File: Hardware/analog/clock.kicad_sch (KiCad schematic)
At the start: 4 parts, among them Y701 25MHz

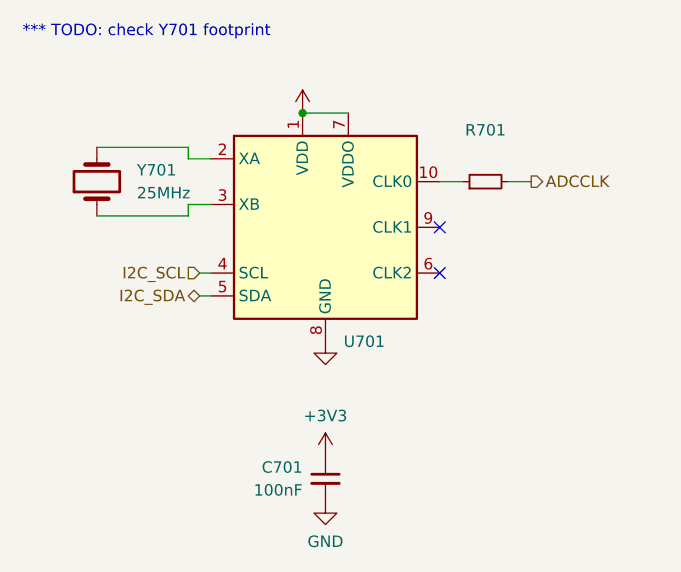
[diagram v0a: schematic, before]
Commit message: Add ADC aliasing filters
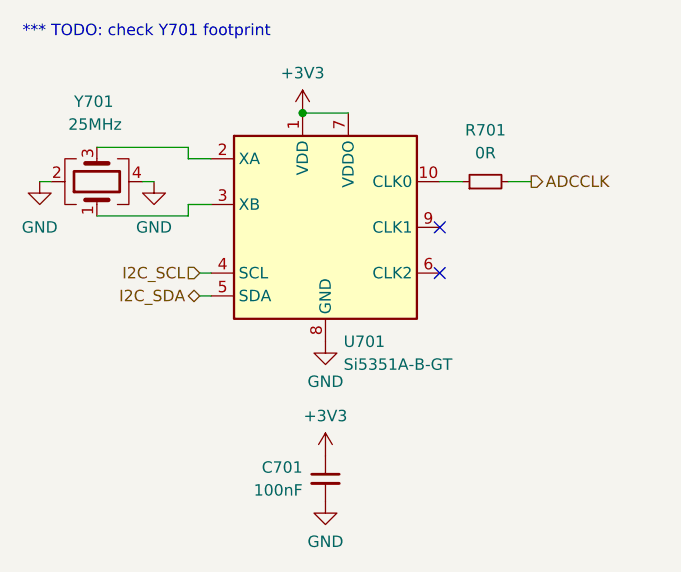
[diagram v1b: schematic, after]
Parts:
- R701: value (none) -> 0R; footprint (none) -> Resistor_SMD:R_0805_2012Metric_Pad1.20x1.40mm_HandSolder
- U701: value (none) -> Si5351A-B-GT; footprint (none) -> Package_SO:MSOP-10_3x3mm_P0.5mm
- Y701: symbol Device:Crystal -> Device:Crystal_GND24
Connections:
- net GND: now also Y701.2, Y701.4
- net at U701.2 (XA): now also Y701.3; no longer Y701.2
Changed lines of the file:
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@@
+    (stroke (width 0) (type default) (color 0 0 0 0))
+  )
+  (wire (pts (xy 29.21 36.83) (xy 30.48 36.83))
     (stroke (width 0) (type default) (color 0 0 0 0))
   )
@@
   )
   (wire (pts (xy 81.28 36.83) (xy 83.82 36.83))
+    (stroke (width 0) (type default) (color 0 0 0 0))
+  )
+  (wire (pts (xy 41.91 36.83) (xy 40.64 36.83))
     (stroke (width 0) (type default) (color 0 0 0 0))
   )
@@
       (effects (font (size 1.27 1.27)) hide)
     )
-    (property "Value" "" (id 1) (at 58.42 24.765 0))
+    (property "Value" "+3V3" (id 1) (at 58.42 24.765 0))
     (property "Footprint" "" (id 2) (at 58.42 29.21 0)
       (effects (font (size 1.27 1.27)) hide)
@@
     (in_bom yes) (on_board yes) (fields_autoplaced)
     (property "Reference" "R701" (id 0) (at 78.74 31.115 90))
-    (property "Value" "" (id 1) (at 78.74 33.655 90))
-    (property "Footprint" "" (id 2) (at 78.74 36.83 0)
+    (property "Value" "0R" (id 1) (at 78.74 33.655 90))
+    (property "Footprint" "Resistor_SMD:R_0805_2012Metric_Pad1.20x1.40mm_HandSolder" (id 2) (at 78.74 36.83 0)
       (effects (font (size 1.27 1.27)) hide)
     )
@@
     (pin "2")
   )
-  (symbol (lib_id "Device:Crystal") (at 35.56 36.83 90) (unit 1)
+  (symbol (lib_id "power:GND") (at 41.91 36.83 0) (mirror y) (unit 1)
     (in_bom yes) (on_board yes) (fields_autoplaced)
-    (property "Reference" "Y701" (id 0) (at 40.005 35.5599 90)
+    (property "Reference" "#PWR0117" (id 0) (at 41.91 43.18 0)
+      (effects (font (size 1.27 1.27)) hide)
+    )
+    (property "Value" "GND" (id 1) (at 41.91 41.91 0))
+    (property "Footprint" "" (id 2) (at 41.91 36.83 0)
+      (effects (font (size 1.27 1.27)) hide)
+    )
+    (property "Datasheet" "" (id 3) (at 41.91 36.83 0)
+      (effects (font (size 1.27 1.27)) hide)
+    )
+    (pin "1")
+  )
+  (symbol (lib_id "Device:Crystal_GND24") (at 35.56 36.83 90) (unit 1)
+    (in_bom yes) (on_board yes)
+    (property "Reference" "Y701" (id 0) (at 33.02 27.94 90)
       (effects (font (size 1.27 1.27)) (justify right))
     )
-    (property "Value" "25MHz" (id 1) (at 40.005 38.0999 90)
+    (property "Value" "25MHz" (id 1) (at 32.385 30.48 90)
       (effects (font (size 1.27 1.27)) (justify right))
     )
@@
     (pin "1")
     (pin "2")
+    (pin "3")
+    (pin "4")
+  )
+  (symbol (lib_id "power:GND") (at 29.21 36.83 0) (unit 1)
+    (in_bom yes) (on_board yes) (fields_autoplaced)
+    (property "Reference" "#PWR0112" (id 0) (at 29.21 43.18 0)
+      (effects (font (size 1.27 1.27)) hide)
+    )
+    (property "Value" "GND" (id 1) (at 29.21 41.91 0))
+    (property "Footprint" "" (id 2) (at 29.21 36.83 0)
+      (effects (font (size 1.27 1.27)) hide)
+    )
+    (property "Datasheet" "" (id 3) (at 29.21 36.83 0)
+      (effects (font (size 1.27 1.27)) hide)
+    )
+    (pin "1")
   )
   (symbol (lib_id "power:GND") (at 60.96 54.61 0) (unit 1)
@@
       (effects (font (size 1.27 1.27)) hide)
     )
-    (property "Value" "" (id 1) (at 60.96 59.055 0))
+    (property "Value" "GND" (id 1) (at 60.96 59.055 0))
     (property "Footprint" "" (id 2) (at 60.96 54.61 0)
       (effects (font (size 1.27 1.27)) hide)
@@
       (effects (font (size 1.27 1.27)) (justify left))
     )
-    (property "Value" "" (id 1) (at 62.9794 57.15 0)
+    (property "Value" "Si5351A-B-GT" (id 1) (at 62.9794 57.15 0)
       (effects (font (size 1.27 1.27)) (justify left))
     )
-    (property "Footprint" "" (id 2) (at 60.96 62.23 0)
+    (property "Footprint" "Package_SO:MSOP-10_3x3mm_P0.5mm" (id 2) (at 60.96 62.23 0)
       (effects (font (size 1.27 1.27)) hide)
     )

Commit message: Initial pass at analog board
- Everything currently in the schematic is routed, and stuff is
  reasonably sanely laid out

- Some compromises: namely, the zero offset doesn't use the DAC
  reference for its positive, but generates a separate 2.5V via the
  shunt diodes; this is then shared between both op-amps. That avoids
  the DAC/ADC reference getting noisified

  Also, we don't have an ADC for measuring the temperature sensors yet,
  and in fact, those aren't routed out (or existent really) yet either

- TODO: add test points for drive voltages and current sense voltages
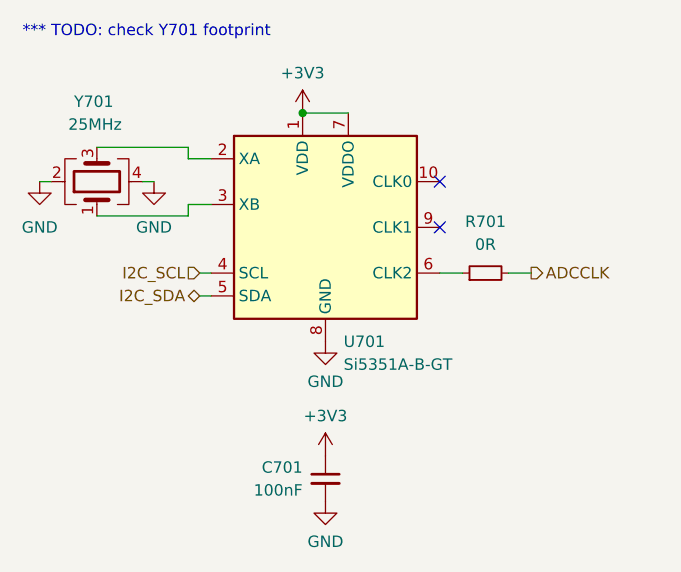
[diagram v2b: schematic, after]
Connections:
- net at R701.1: now also U701.6 (CLK2); no longer U701.10 (CLK0)
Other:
- title: (none) -> 300W Analog Load Board
- moved on the sheet: R701
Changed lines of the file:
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@@
 (kicad_sch (version 20211123) (generator eeschema)
   (paper "A4")
+  (title_block
+    (title "300W Analog Load Board")
+    (rev "1")
+  )
   (junction (at 58.42 29.21) (diameter 0) (color 0 0 0 0)
   )
-  (no_connect (at 73.66 46.99))
   (no_connect (at 73.66 41.91))
+  (no_connect (at 73.66 36.83))
   (wire (pts (xy 45.72 39.37) (xy 48.26 39.37))
     (stroke (width 0) (type default) (color 0 0 0 0))
@@
     (stroke (width 0) (type default) (color 0 0 0 0))
   )
-  (wire (pts (xy 81.28 36.83) (xy 83.82 36.83))
+  (wire (pts (xy 81.28 46.99) (xy 83.82 46.99))
     (stroke (width 0) (type default) (color 0 0 0 0))
   )
   (wire (pts (xy 41.91 36.83) (xy 40.64 36.83))
-    (stroke (width 0) (type default) (color 0 0 0 0))
-  )
-  (wire (pts (xy 73.66 36.83) (xy 76.2 36.83))
     (stroke (width 0) (type default) (color 0 0 0 0))
   )
@@
   )
   (wire (pts (xy 58.42 29.21) (xy 63.5 29.21))
+    (stroke (width 0) (type default) (color 0 0 0 0))
+  )
+  (wire (pts (xy 73.66 46.99) (xy 76.2 46.99))
     (stroke (width 0) (type default) (color 0 0 0 0))
   )
@@
     (effects (font (size 1.27 1.27)) (justify right))
   )
-  (hierarchical_label "ADCCLK" (shape output) (at 83.82 36.83 0)
+  (hierarchical_label "ADCCLK" (shape output) (at 83.82 46.99 0)
     (effects (font (size 1.27 1.27)) (justify left))
   )
@@
     (pin "2")
   )
-  (symbol (lib_id "Device:R_Small") (at 78.74 36.83 90) (unit 1)
+  (symbol (lib_id "Device:R_Small") (at 78.74 46.99 90) (unit 1)
     (in_bom yes) (on_board yes) (fields_autoplaced)
-    (property "Reference" "R701" (id 0) (at 78.74 31.115 90))
-    (property "Value" "0R" (id 1) (at 78.74 33.655 90))
-    (property "Footprint" "Resistor_SMD:R_0805_2012Metric_Pad1.20x1.40mm_HandSolder" (id 2) (at 78.74 36.83 0)
+    (property "Reference" "R701" (id 0) (at 78.74 41.275 90))
+    (property "Value" "0R" (id 1) (at 78.74 43.815 90))
+    (property "Footprint" "Resistor_SMD:R_0805_2012Metric_Pad1.20x1.40mm_HandSolder" (id 2) (at 78.74 46.99 0)
       (effects (font (size 1.27 1.27)) hide)
     )
-    (property "Datasheet" "~" (id 3) (at 78.74 36.83 0)
+    (property "Datasheet" "~" (id 3) (at 78.74 46.99 0)
       (effects (font (size 1.27 1.27)) hide)
     )

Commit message: Added more decoupling for reference
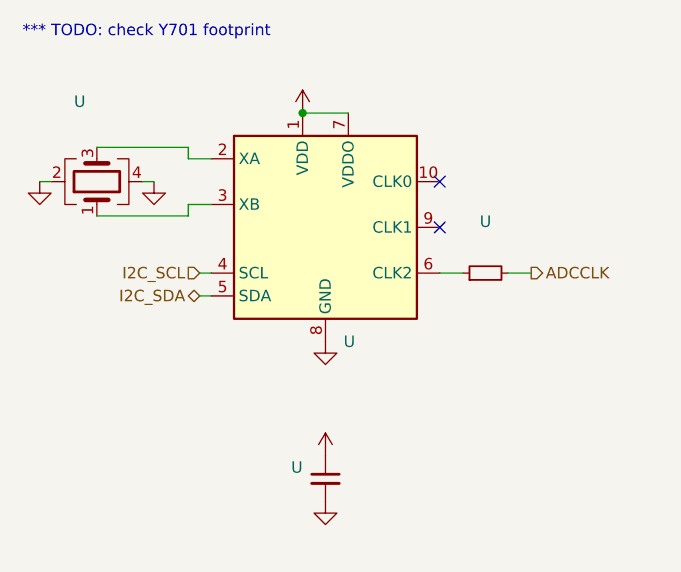
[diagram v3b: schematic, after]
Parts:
- U: renamed from C701; value 100nF -> (none); footprint Capacitor_SMD:C_0805_2012Metric_Pad1.18x1.45mm_HandSolder -> (none)
- U: renamed from R701; value 0R -> (none); footprint Resistor_SMD:R_0805_2012Metric_Pad1.20x1.40mm_HandSolder -> (none)
- U: renamed from Y701; value 25MHz -> (none); footprint Crystal:Crystal_SMD_SeikoEpson_TSX3225-4Pin_3.2x2.5mm_HandSoldering -> (none)
- U: renamed from U701; value Si5351A-B-GT -> (none); footprint Package_SO:MSOP-10_3x3mm_P0.5mm -> (none)

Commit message: Analog board layout
- Started work on adding the voltage sense circuitry, including the
  selector relay, IO expander to drive the relay, and the second ADC to
  convert the voltage values

- Changed the layout of analog board to better take advantage of
  available space

- Minor changes to front panel layout for aesthetics
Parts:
- added U: (no value), symbol Device:R_Small
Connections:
- net at U.9 (CLK1): now also U.1
- net ADCCLK renamed ADCCLK_{0}
- new net ADCCLK_{1}: U.2
- no-connect marks 2 -> 1
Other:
- moved on the sheet: U
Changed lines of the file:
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@@
   (junction (at 58.42 29.21) (diameter 0) (color 0 0 0 0)
   )
-  (no_connect (at 73.66 41.91))
   (no_connect (at 73.66 36.83))
   (wire (pts (xy 45.72 39.37) (xy 48.26 39.37))
+    (stroke (width 0) (type default))
+  )
+  (wire (pts (xy 73.66 46.99) (xy 74.93 46.99))
     (stroke (width 0) (type default))
   )
@@
     (stroke (width 0) (type default))
   )
-  (wire (pts (xy 81.28 46.99) (xy 83.82 46.99))
+  (wire (pts (xy 81.28 49.53) (xy 83.82 49.53))
     (stroke (width 0) (type default))
   )
@@
     (stroke (width 0) (type default))
   )
+  (wire (pts (xy 74.93 46.99) (xy 74.93 49.53))
+    (stroke (width 0) (type default))
+  )
   (wire (pts (xy 46.99 49.53) (xy 48.26 49.53))
+    (stroke (width 0) (type default))
+  )
+  (wire (pts (xy 74.93 49.53) (xy 76.2 49.53))
     (stroke (width 0) (type default))
   )
@@
     (stroke (width 0) (type default))
   )
-  (wire (pts (xy 73.66 46.99) (xy 76.2 46.99))
+  (wire (pts (xy 81.28 41.91) (xy 83.82 41.91))
     (stroke (width 0) (type default))
   )
   (wire (pts (xy 45.72 40.64) (xy 45.72 39.37))
+    (stroke (width 0) (type default))
+  )
+  (wire (pts (xy 73.66 41.91) (xy 76.2 41.91))
     (stroke (width 0) (type default))
   )
@@
     (effects (font (size 1.27 1.27)) (justify left bottom))
   )
+  (hierarchical_label "ADCCLK_{1}" (shape output) (at 83.82 41.91 0) (fields_autoplaced)
+    (effects (font (size 1.27 1.27)) (justify left))
+  )
   (hierarchical_label "I2C_SDA" (shape bidirectional) (at 46.99 49.53 180) (fields_autoplaced)
     (effects (font (size 1.27 1.27)) (justify right))
@@
     (effects (font (size 1.27 1.27)) (justify right))
   )
-  (hierarchical_label "ADCCLK" (shape output) (at 83.82 46.99 0) (fields_autoplaced)
+  (hierarchical_label "ADCCLK_{0}" (shape output) (at 83.82 49.53 0) (fields_autoplaced)
     (effects (font (size 1.27 1.27)) (justify left))
   )
@@
     (pin "2")
   )
-  (symbol (lib_id "Device:R_Small") (at 78.74 46.99 90) (unit 1)
-    (in_bom yes) (on_board yes) (fields_autoplaced)
+  (symbol (lib_id "Device:R_Small") (at 78.74 41.91 90) (unit 1)
+    (in_bom yes) (on_board yes)
     (default_instance (reference "U") (unit 1) (value "") (footprint ""))
-    (property "Reference" "U" (id 0) (at 78.74 41.275 90)
+    (property "Reference" "U" (id 0) (at 78.74 37.465 90)
       (effects (font (size 1.27 1.27)))
     )
-    (property "Value" "" (id 1) (at 78.74 43.815 90)
+    (property "Value" "" (id 1) (at 78.74 40.005 90)
       (effects (font (size 1.27 1.27)))
     )
-    (property "Footprint" "" (id 2) (at 78.74 46.99 0)
+    (property "Footprint" "" (id 2) (at 78.74 41.91 0)
       (effects (font (size 1.27 1.27)) hide)
     )
-    (property "Datasheet" "~" (id 3) (at 78.74 46.99 0)
+    (property "Datasheet" "~" (id 3) (at 78.74 41.91 0)
       (effects (font (size 1.27 1.27)) hide)
     )
+    (pin "1")
+    (pin "2")
+  )
+  (symbol (lib_id "Device:R_Small") (at 78.74 49.53 90) (unit 1)
+    (in_bom yes) (on_board yes)
+    (default_instance (reference "U") (unit 1) (value "") (footprint ""))
+    (property "Reference" "U" (id 0) (at 78.74 45.085 90)
+      (effects (font (size 1.27 1.27)))
+    )
+    (property "Value" "" (id 1) (at 78.74 47.625 90)
+      (effects (font (size 1.27 1.27)))
+    )
+    (property "Footprint" "" (id 2) (at 78.74 49.53 0)
+      (effects (font (size 1.27 1.27)) hide)
+    )
+    (property "Datasheet" "~" (id 3) (at 78.74 49.53 0)
+      (effects (font (size 1.27 1.27)) hide)
+    )

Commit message: Temperature sensing & cleanup for analog board
- Added the auxiliary temperature sensing ADC, and routed it to the
  analog temperature sensors on the front and rear of the MOSFET
  heatsink

- Added an LM75 sensor to measure the analog board ambient temperature
  (for better temperature control/fan control)

  This may end up being a DNP item if it's not really useful or
  otherwise necessary.

- Fixes to a few symbols (namely pin directions) to pass ERC
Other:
- note added: "I2C Address: 0b1100000"
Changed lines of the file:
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@@
+    (effects (font (size 1.27 1.27)) (justify left bottom))
+  )
+  (text "I2C Address: 0b1100000" (at 27.94 22.86 0)
     (effects (font (size 1.27 1.27)) (justify left bottom))
   )
